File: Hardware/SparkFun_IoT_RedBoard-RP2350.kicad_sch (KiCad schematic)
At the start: 39 parts, among them J1 Conn_01x08_SMD_Combined, J10 Conn_01x03, J11 Conn_01x22_FPC_0.5mm_HSTX_Ver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, J12 Qwiic_RA, J14 JST_1mm_3_Vertical, J2 Conn_01x06_SMD_Combined, J3 Barrel_Jack_SMD, J4 USB_C_Receptacle, J5 Conn_01x04_SolderPads, J6 Conn_01x02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

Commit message: Update v01 from checklist. Added measures.
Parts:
- J1, J9: PROD_ID (none) -> CONN-10204
- J11: PROD_ID (none) -> CONN-24643
- J12: renamed from J14; PROD_ID CONN- -> CONN-24642
- J2: PROD_ID (none) -> CONN-10203
- J8: PROD_ID (none) -> CONN-11219
- renumbered J12 to J13
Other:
- note added: "VIN: 7-15V"
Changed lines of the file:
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@@
 		)
 	)
+	(text "VIN: 7-15V"
+		(exclude_from_sim no)
+		(at 44.45 158.115 0)
+		(effects
+			(font
+				(size 1.27 1.27)
+			)
+		)
+	)
 	(text "Debug Header"
 		(exclude_from_sim no)
@@
 		(dnp no)
 		(fields_autoplaced yes)
-		(property "Reference" "#PWR022"
+		(property "Reference" "#PWR023"
 			(at 367.03 186.69 0)
 			(effects
@@
 			(project "SparkFun_IoT_RedBoard-RP2350"
 				(path "/e3dd3ae4-244d-4cba-9cca-5d2abf83f29a"
-					(reference "#PWR022")
+					(reference "#PWR023")
 					(unit 1)
 				)
@@
 			)
 		)
-		(pin "C"
-		)
 		(pin "A"
 		)
+		(pin "C"
+		)
 		(instances
 			(project ""
@@
 		(dnp no)
 		(fields_autoplaced yes)
-		(property "Reference" "#PWR026"
+		(property "Reference" "#PWR027"
 			(at 381 199.39 0)
 			(effects
@@
 			(project "SparkFun_IoT_RedBoard-RP2350"
 				(path "/e3dd3ae4-244d-4cba-9cca-5d2abf83f29a"
-					(reference "#PWR026")
+					(reference "#PWR027")
 					(unit 1)
 				)
@@
 			)
 		)
+		(property "PROD_ID" "CONN-11219"
+			(at 176.784 238.76 0)
+			(effects
+				(font
+					(size 1.27 1.27)
+				)
+				(hide yes)
+			)
+		)
 		(pin "1"
 		)
@@
 			)
 		)
+		(property "PROD_ID" "CONN-24643"
+			(at 381.254 73.914 0)
+			(effects
+				(font
+					(size 1.27 1.27)
+				)
+				(hide yes)
+			)
+		)
 		(pin "7"
 		)
@@
 		(on_board yes)
 		(dnp no)
-		(property "Reference" "#PWR023"
+		(property "Reference" "#PWR022"
 			(at 364.49 50.8 0)
 			(effects
@@
 			(project "SparkFun_IoT_RedBoard-RP2350"
 				(path "/e3dd3ae4-244d-4cba-9cca-5d2abf83f29a"
-					(reference "#PWR023")
+					(reference "#PWR022")
 					(unit 1)
 				)
@@
 		(dnp no)
 		(fields_autoplaced yes)
-		(property "Reference" "J14"
+		(property "Reference" "J12"
 			(at 389.89 36.8299 0)
 			(effects
@@
 			)
 		)
-		(property "Datasheet" "https://www.jst.com/wp-content/uploads/2021/03/eSR_SZ-new.pdf"
+		(property "Datasheet" "http://www.4uconnector.com/online/object/4udrawing/07265.pdf"
 			(at 384.81 49.53 0)
 			(effects
@@
 			)
 		)
-		(property "PROD_ID" "CONN-"
+		(property "PROD_ID" "CONN-24642"
 			(at 384.81 52.07 0)
 			(effects
@@
 			(project ""
 				(path "/e3dd3ae4-244d-4cba-9cca-5d2abf83f29a"
-					(reference "J14")
+					(reference "J12")
 					(unit 1)
 				)
@@
 		(on_board yes)
 		(dnp no)
-		(property "Reference" "#PWR0126"
+		(property "Reference" "#PWR026"
 			(at 378.46 50.8 0)
 			(effects
@@
 			(project "SparkFun_IoT_RedBoard-RP2350"
 				(path "/e3dd3ae4-244d-4cba-9cca-5d2abf83f29a"
-					(reference "#PWR0126")
+					(reference "#PWR026")
 					(unit 1)
 				)
@@
 			)
 		)
+		(property "PROD_ID" "CONN-10204"
+			(at 176.784 268.986 0)
+			(effects
+				(font
+					(size 1.27 1.27)
+				)
+				(hide yes)
+			)
+		)
 		(pin "5"
 		)
@@
 		(on_board yes)
 		(dnp no)
-		(property "Reference" "J12"
+		(property "Reference" "J13"
 			(at 387.985 193.675 0)
 			(effects
@@
 			(project ""
 				(path "/e3dd3ae4-244d-4cba-9cca-5d2abf83f29a"
-					(reference "J12")
+					(reference "J13")
 					(unit 1)
 				)
@@
 			)
 		)
+		(property "PROD_ID" "CONN-10204"
+			(at 42.926 238.506 0)
+			(effects
+				(font
+					(size 1.27 1.27)
+				)
+				(hide yes)
+			)
+		)
 		(pin "1"
 		)
@@
 		(on_board yes)
 		(dnp no)
-		(property "Reference" "#PWR027"
+		(property "Reference" "#PWR028"
 			(at 381 213.36 0)
 			(effects
@@
 			(project "SparkFun_IoT_RedBoard-RP2350"
 				(path "/e3dd3ae4-244d-4cba-9cca-5d2abf83f29a"
-					(reference "#PWR027")
+					(reference "#PWR028")
 					(unit 1)
 				)
@@
 			(effects
 				(font
+					(size 1.27 1.27)
+				)
+				(hide yes)
+			)
+		)
+		(property "PROD_ID" "CONN-10203"
+			(at 42.926 274.32 0)
+			(effects
+				(font

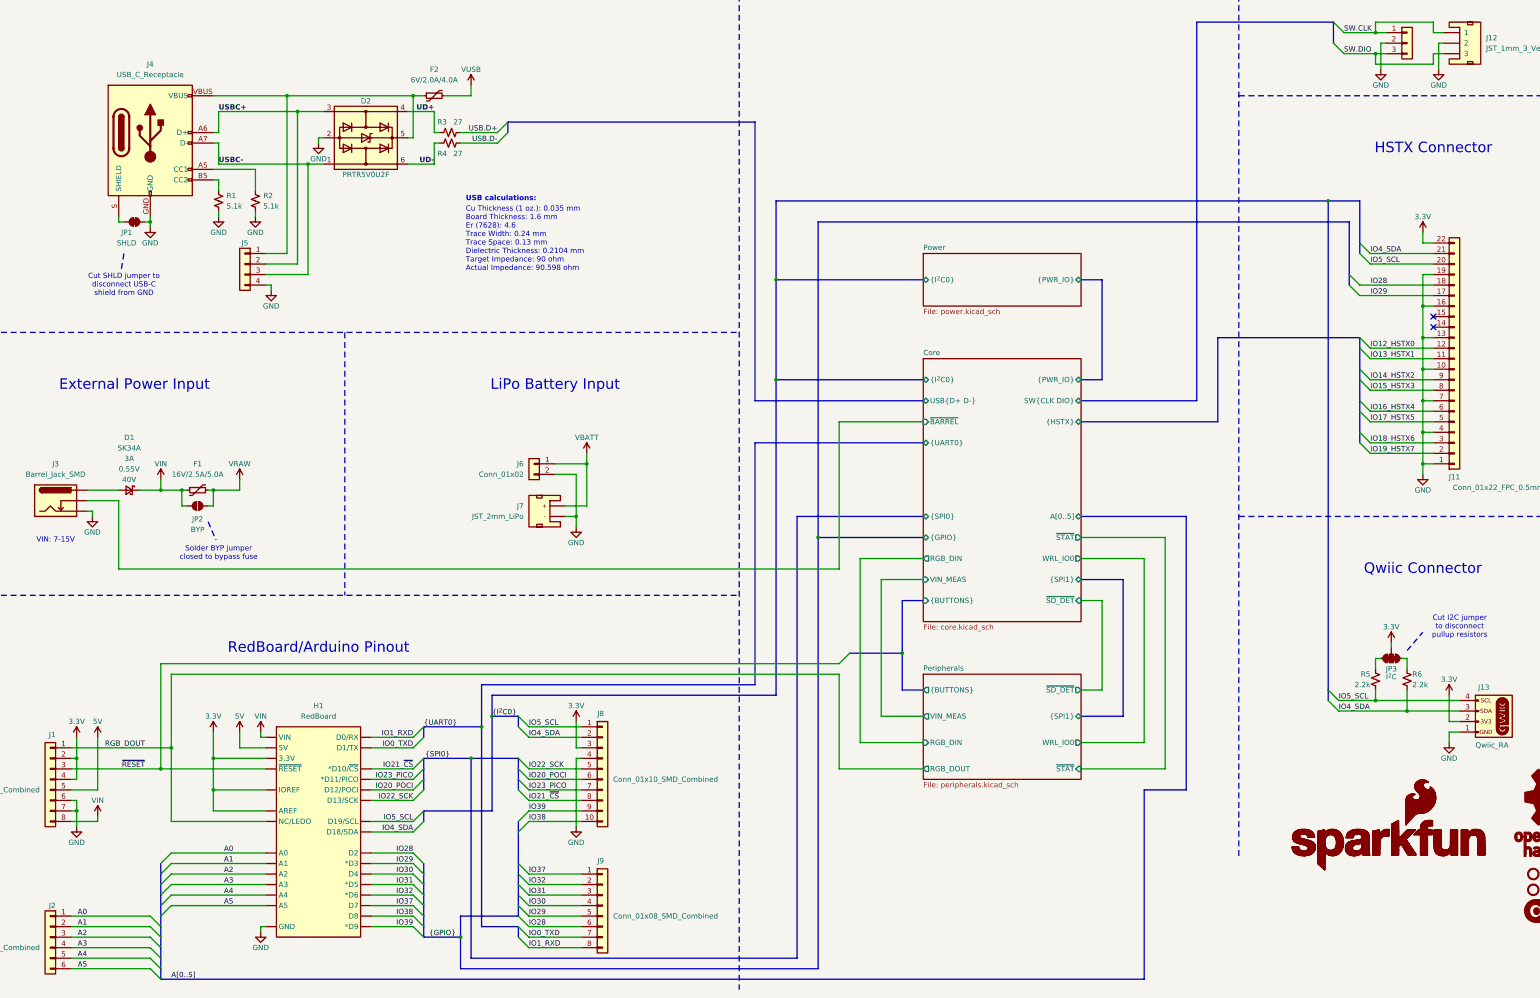
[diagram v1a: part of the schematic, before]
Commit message: v01 post design review changes. Panelize/CAM.
Remove F3.
Added switched power for qwiic, rgb, sd.
Update USB diode for prod friendly package.
Added debounce cap on User button.
Swap user and boot buttons.
Make F2 a smaller package.
Renumber GPIO and use contiguous numbers for PIO purposes.
Swap inputs on Ideal diodes for battery powered current purposes.
Move USB termination resistors closer to MCU.
Fixed A0-A5 ordering.
Update silks.
Add mask to middle of SMD GPIOs.
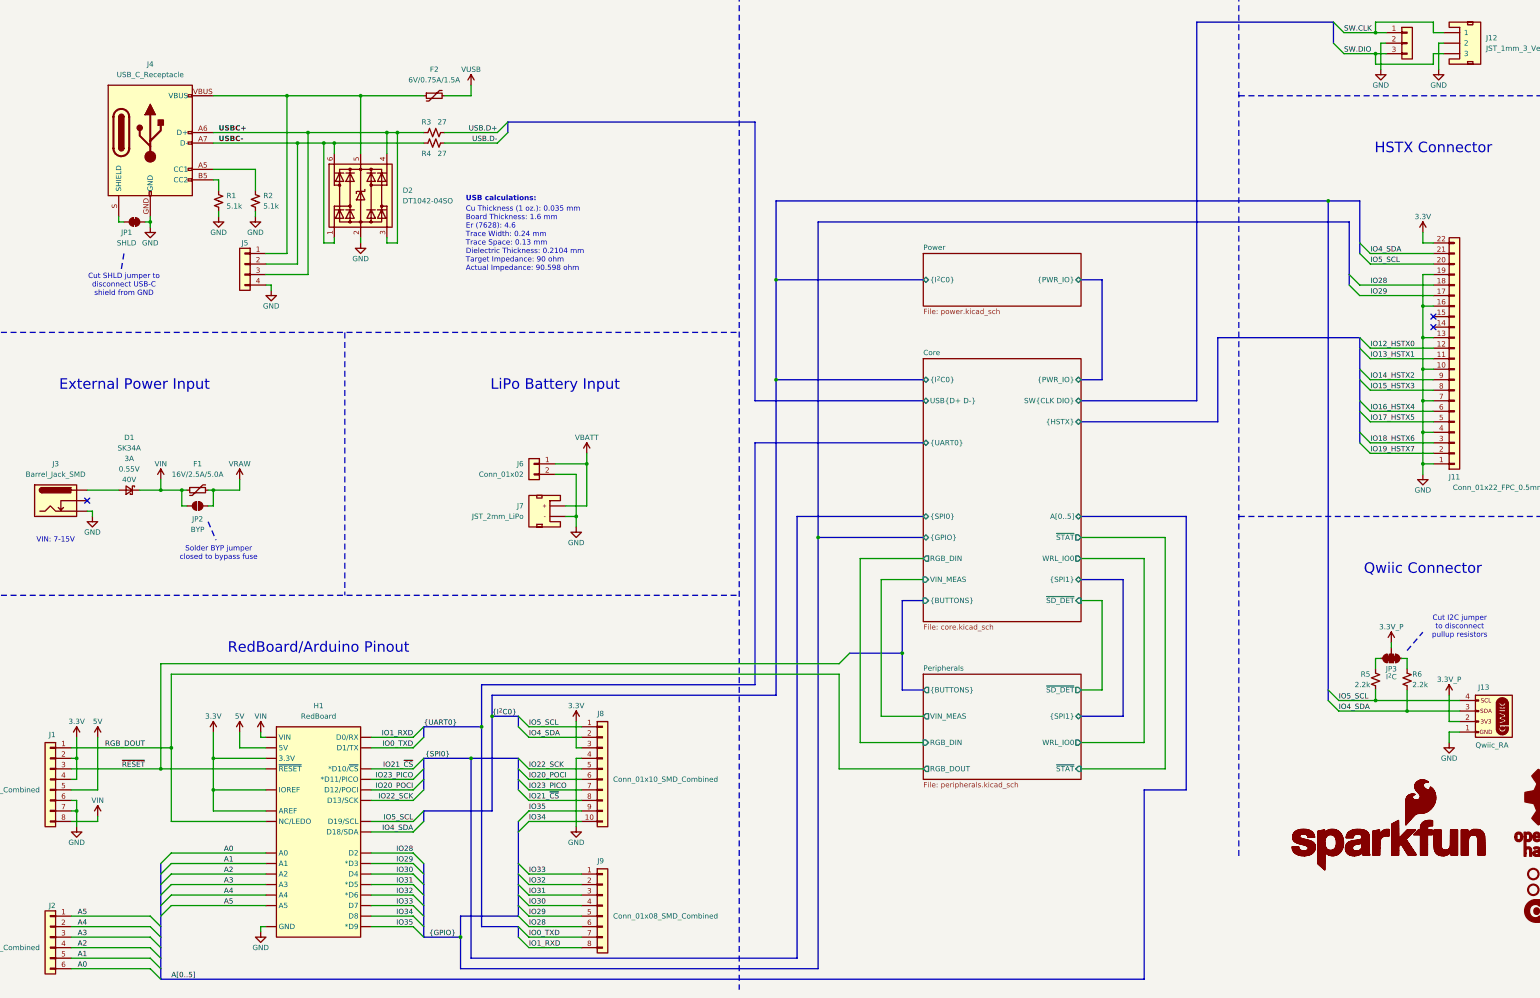
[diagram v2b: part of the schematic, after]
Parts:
- removed D2: PRTR5V0U2F, Package_TO_SOT_SMD:SOT-886, symbol SparkFun-DiscreteSemi:D_TVS_ESD_USB_SOT886
- added D2: DT1042-04SO, SparkFun-Semiconductor-Standard:SOT23-6, symbol SparkFun-DiscreteSemi:D_TVS_ESD_USB
- F2: value 6V/2.0A/4.0A -> 6V/0.75A/1.5A; footprint SparkFun-Fuse:1210 -> SparkFun-Fuse:1206; symbol SparkFun-Fuse:Fuse 6V/2.0A/4.0A -> SparkFun-Fuse:Fuse 6V/0.75A/1.5A; PROD_ID RES-14313 -> RES-11150
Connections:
- net UD+ is gone; now on net USBC+: R3.1
- net UD- is gone; now on net USBC-: R4.1
- net 3.3V: no longer J13.2 (Pin_2), JP3.2 (B)
- net A0: now also J2.6 (Pin_6); no longer J2.1 (Pin_1)
- net A1: now also J2.5 (Pin_5); no longer J2.2 (Pin_2)
- net A2: now also J2.4 (Pin_4); no longer J2.3 (Pin_3)
- net A3: now also J2.3 (Pin_3); no longer J2.4 (Pin_4)
- net A4: now also J2.2 (Pin_2); no longer J2.5 (Pin_5)
- net A5: now also J2.1 (Pin_1); no longer J2.6 (Pin_6)
- net GND: now also D2.2 (GND)
- net USBC+: now also J5.3 (Pin_3), D2.3 (I/O2), D2.4 (I/O3); no longer J5.2 (Pin_2)
- net USBC-: now also J5.2 (Pin_2), D2.1 (I/O1), D2.6 (I/O4); no longer J5.3 (Pin_3)
- net at F2.1, J4.VBUS, J5.1 (Pin_1): now also D2.5 (VCC)
- net Core/~{BARREL}: no longer names the net of J3.GNDBREAK
- net IO37 renamed IO33
- net IO38 renamed IO34
- net IO39 renamed IO35
- new net 3.3V_P: J13.2 (Pin_2), JP3.2 (B)
- no-connect marks 2 -> 3
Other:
- sheet Core ports: added none; removed ~{BARREL}
- moved on the sheet: R3, R4

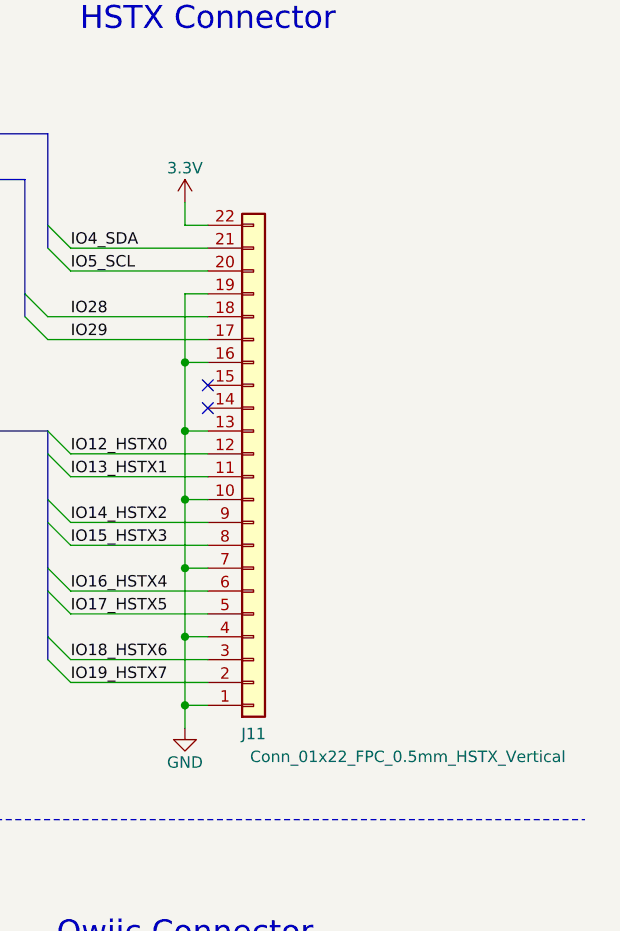
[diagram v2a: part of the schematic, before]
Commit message: Update for reds
Change version number to v10.
Make user button number correct.
Rotate HSTX conn 180 degrees electrically.
Add silk for HSTX contact direction.
Increase silk text size where it made sense.
Increase silk label length on PTHs.
Panelize and CAM.
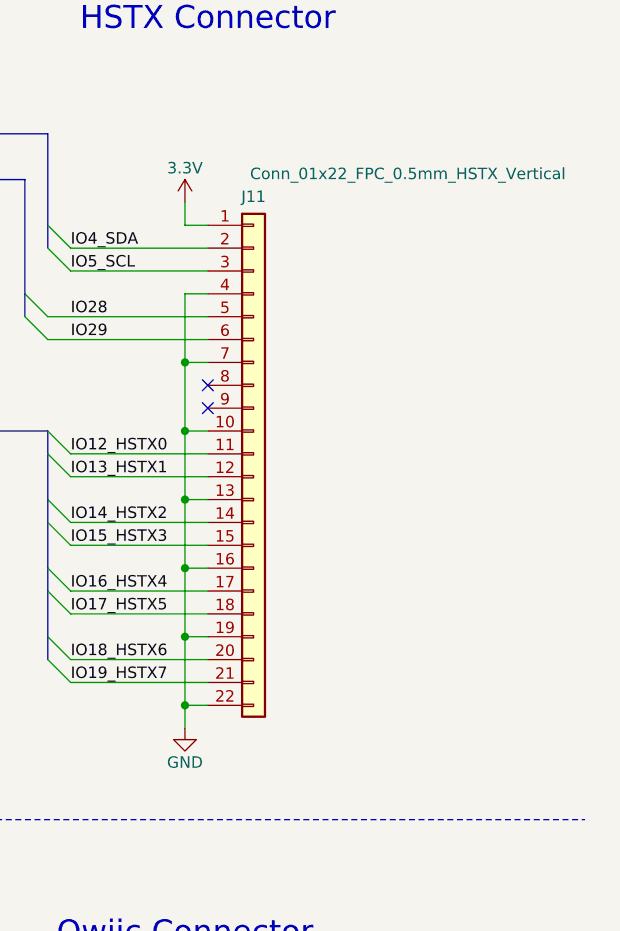
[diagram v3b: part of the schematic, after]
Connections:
- net 3.3V: now also J11.1 (Pin_1); no longer J11.22 (Pin_22)
- net GND: now also J11.22 (Pin_22); no longer J11.1 (Pin_1)
- net IO12_HSTX0: now also J11.11 (Pin_11); no longer J11.12 (Pin_12)
- net IO13_HSTX1: now also J11.12 (Pin_12); no longer J11.11 (Pin_11)
- net IO14_HSTX2: now also J11.14 (Pin_14); no longer J11.9 (Pin_9)
- net IO15_HSTX3: now also J11.15 (Pin_15); no longer J11.8 (Pin_8)
- net IO16_HSTX4: now also J11.17 (Pin_17); no longer J11.6 (Pin_6)
- net IO17_HSTX5: now also J11.18 (Pin_18); no longer J11.5 (Pin_5)
- net IO18_HSTX6: now also J11.20 (Pin_20); no longer J11.3 (Pin_3)
- net IO19_HSTX7: now also J11.21 (Pin_21); no longer J11.2 (Pin_2)
- net IO28: now also J11.5 (Pin_5); no longer J11.18 (Pin_18)
- net IO29: now also J11.6 (Pin_6); no longer J11.17 (Pin_17)
- net IO4_SDA: now also J11.2 (Pin_2); no longer J11.21 (Pin_21)
- net IO5_SCL: now also J11.3 (Pin_3); no longer J11.20 (Pin_20)
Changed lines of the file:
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@@
 	(title_block
 		(title "SparkFun IoT RedBoard - RP2350 - Top Level/Connectors")
-		(date "2024-12-03")
-		(rev "v01")
+		(date "2025-02-05")
+		(rev "v10")
 		(company "SparkFun Electronics")
 		(comment 1 "Designed by: Alex Brudner")
@@
 	)
 	(symbol
+		(lib_id "SparkFun-Connector:Conn_01x22_FPC_0.5mm_HSTX_Vertical")
+		(at 382.27 111.76 0)
+		(unit 1)
+		(exclude_from_sim no)
+		(in_bom yes)
+		(on_board yes)
+		(dnp no)
+		(property "Reference" "J11"
+			(at 382.27 83.185 0)
+			(effects
+				(font
+					(size 1.27 1.27)
+				)
+			)
+		)
+		(property "Value" "Conn_01x22_FPC_0.5mm_HSTX_Vertical"
+			(at 399.415 80.645 0)
+			(effects
+				(font
+					(size 1.27 1.27)
+				)
+			)
+		)
+		(property "Footprint" "SparkFun-Connector:FPC_0.5mm-22_Vertical"
+			(at 382.27 144.78 0)
+			(effects
+				(font
+					(size 1.27 1.27)
+				)
+				(hide yes)
+			)
+		)
+		(property "Datasheet" "https://www.cvilux.com/uploads/drawings/100/332/CF2081S.pdf"
+			(at 382.27 147.32 0)
+			(effects
+				(font
+					(size 1.27 1.27)
+				)
+				(hide yes)
+			)
+		)
+		(property "Description" "Generic connector, single row, 01x22, script generated (kicad-library-utils/schlib/autogen/connector/)"
+			(at 382.27 149.86 0)
+			(effects
+				(font
+					(size 1.27 1.27)
+				)
+				(hide yes)
+			)
+		)
+		(property "PROD_ID" "CONN-24643"
+			(at 381.254 152.146 0)
+			(effects
+				(font
+					(size 1.27 1.27)
+				)
+				(hide yes)
+			)
+		)
+		(pin "7"
+		)
+		(pin "2"
+		)
+		(pin "8"
+		)
+		(pin "13"
+		)
+		(pin "14"
+		)
+		(pin "17"
+		)
+		(pin "18"
+		)
+		(pin "21"
+		)
+		(pin "6"
+		)
+		(pin "9"
+		)
+		(pin "1"
+		)
+		(pin "11"
+		)
+		(pin "15"
+		)
+		(pin "12"
+		)
+		(pin "16"
+		)
+		(pin "19"
+		)
+		(pin "10"
+		)
+		(pin "22"
+		)
+		(pin "4"
+		)
+		(pin "20"
+		)
+		(pin "3"
+		)
+		(pin "5"
+		)
+		(instances
+			(project "SparkFun_IoT_RedBoard-RP2350"
+				(path "/e3dd3ae4-244d-4cba-9cca-5d2abf83f29a"
+					(reference "J11")
+					(unit 1)
+				)
+			)
+		)
+	)
+	(symbol
 		(lib_id "power:GND")
 		(at 49.53 227.33 0)
@@
 					(unit 1)
 				)
-			)
-		)
-	)
-	(symbol
-		(lib_id "SparkFun-Connector:Conn_01x22_FPC_0.5mm_HSTX_Vertical")
-		(at 382.27 114.3 0)
-		(mirror x)
-		(unit 1)
-		(exclude_from_sim no)
-		(in_bom yes)
-		(on_board yes)
-		(dnp no)
-		(property "Reference" "J11"
-			(at 382.27 142.875 0)
-			(effects
-				(font
-					(size 1.27 1.27)
-				)
-			)
-		)
-		(property "Value" "Conn_01x22_FPC_0.5mm_HSTX_Vertical"
-			(at 399.415 145.415 0)
-			(effects
-				(font
-					(size 1.27 1.27)
-				)
-			)
-		)
-		(property "Footprint" "SparkFun-Connector:FPC_0.5mm-22_Vertical"
-			(at 382.27 81.28 0)
-			(effects
-				(font
-					(size 1.27 1.27)
-				)
-				(hide yes)
-			)
-		)
-		(property "Datasheet" "https://www.cvilux.com/uploads/drawings/100/332/CF2081S.pdf"
-			(at 382.27 78.74 0)
-			(effects
-				(font
-					(size 1.27 1.27)
-				)
-				(hide yes)
-			)
-		)
-		(property "Description" "Generic connector, single row, 01x22, script generated (kicad-library-utils/schlib/autogen/connector/)"
-			(at 382.27 76.2 0)
-			(effects
-				(font
-					(size 1.27 1.27)
-				)
-				(hide yes)
-			)
-		)
-		(property "PROD_ID" "CONN-24643"
-			(at 381.254 73.914 0)
-			(effects
-				(font
-					(size 1.27 1.27)
-				)
-				(hide yes)
-			)
-		)
-		(pin "7"
-		)
-		(pin "2"
-		)
-		(pin "8"
-		)
-		(pin "13"
-		)
-		(pin "14"
-		)
-		(pin "17"
-		)
-		(pin "18"
-		)
-		(pin "21"
-		)
-		(pin "6"
-		)
-		(pin "9"
-		)
-		(pin "1"
-		)
-		(pin "11"
-		)
-		(pin "15"
-		)
-		(pin "12"
-		)
-		(pin "16"
-		)
-		(pin "19"
-		)
-		(pin "10"
-		)
-		(pin "22"
-		)
-		(pin "4"
-		)
-		(pin "20"
-		)
-		(pin "3"
-		)
-		(pin "5"
-		)
-		(instances
-			(project ""
-				(path "/e3dd3ae4-244d-4cba-9cca-5d2abf83f29a"
-					(reference "J11")
-					(unit 1)
-				)

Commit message: Update post reds review
Added SOT489
Move vias around so they don't interfere with silk
Change Barrel Jack voltage range.
Increase VUSB trace width.
Add silk to HSTX connector.
Panelize & CAM.
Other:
- note added: "VIN: 6-15V"
- note removed: "VIN: 7-15V"
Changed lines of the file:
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@@
 		)
 	)
-	(text "VIN: 7-15V"
+	(text "VIN: 6-15V"
 		(exclude_from_sim no)
 		(at 44.45 158.115 0)
